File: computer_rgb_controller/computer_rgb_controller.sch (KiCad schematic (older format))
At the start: 19 parts

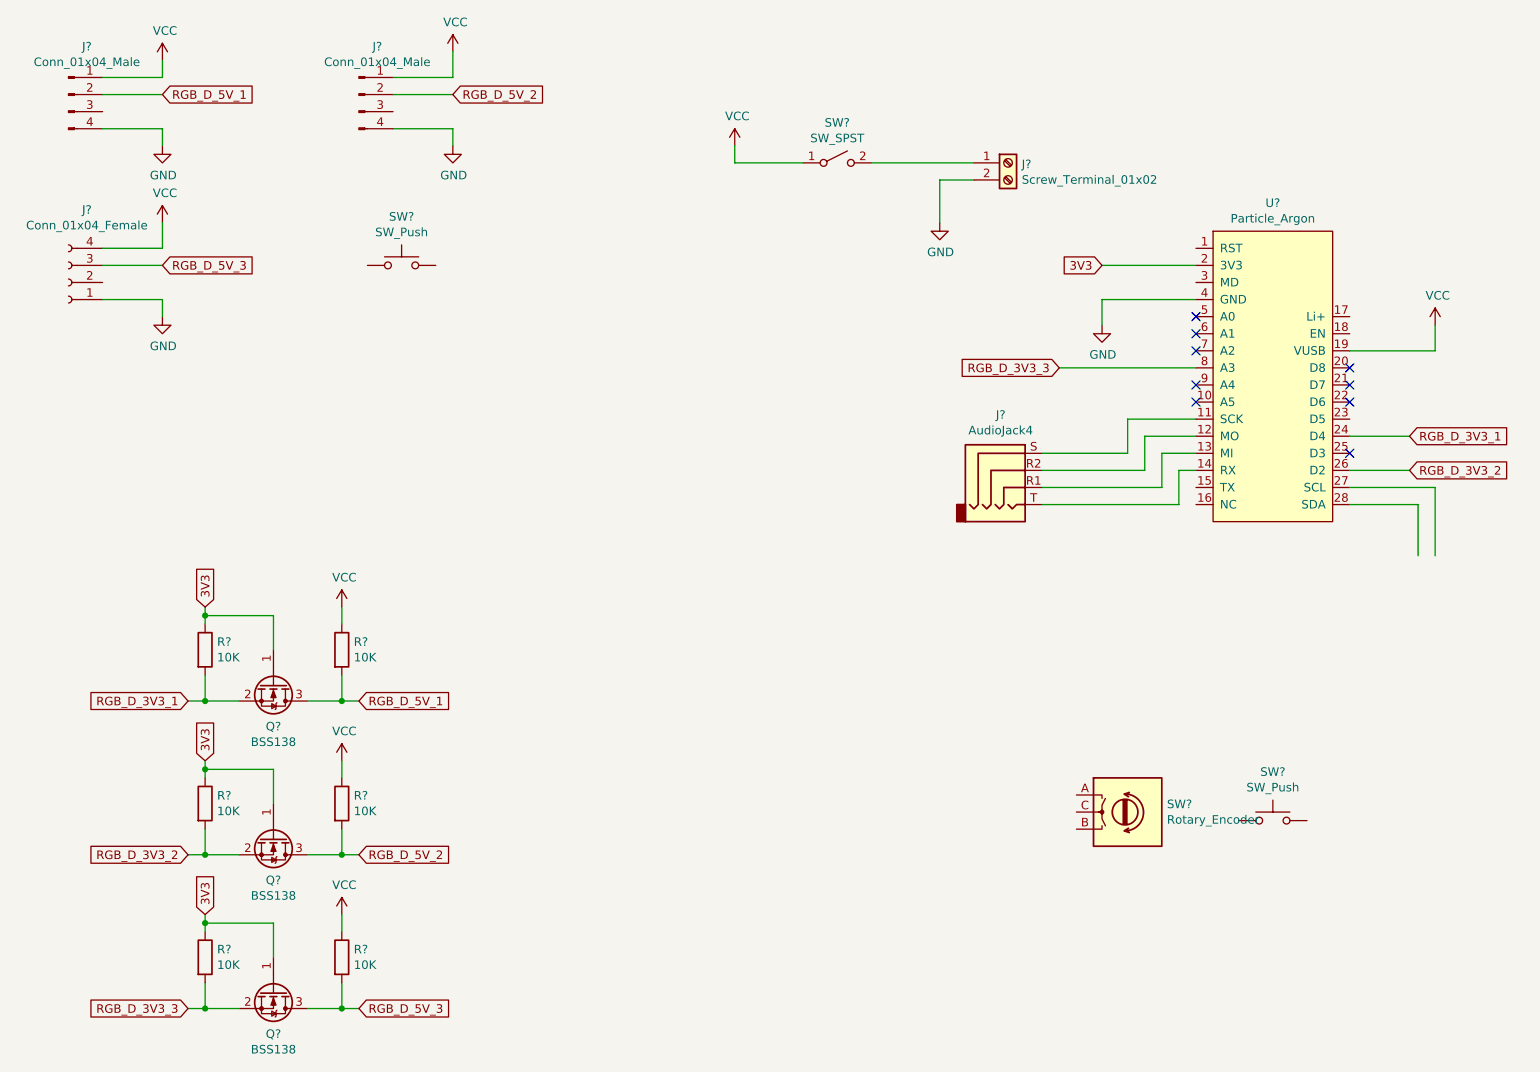
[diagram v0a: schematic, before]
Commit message: added to schematic
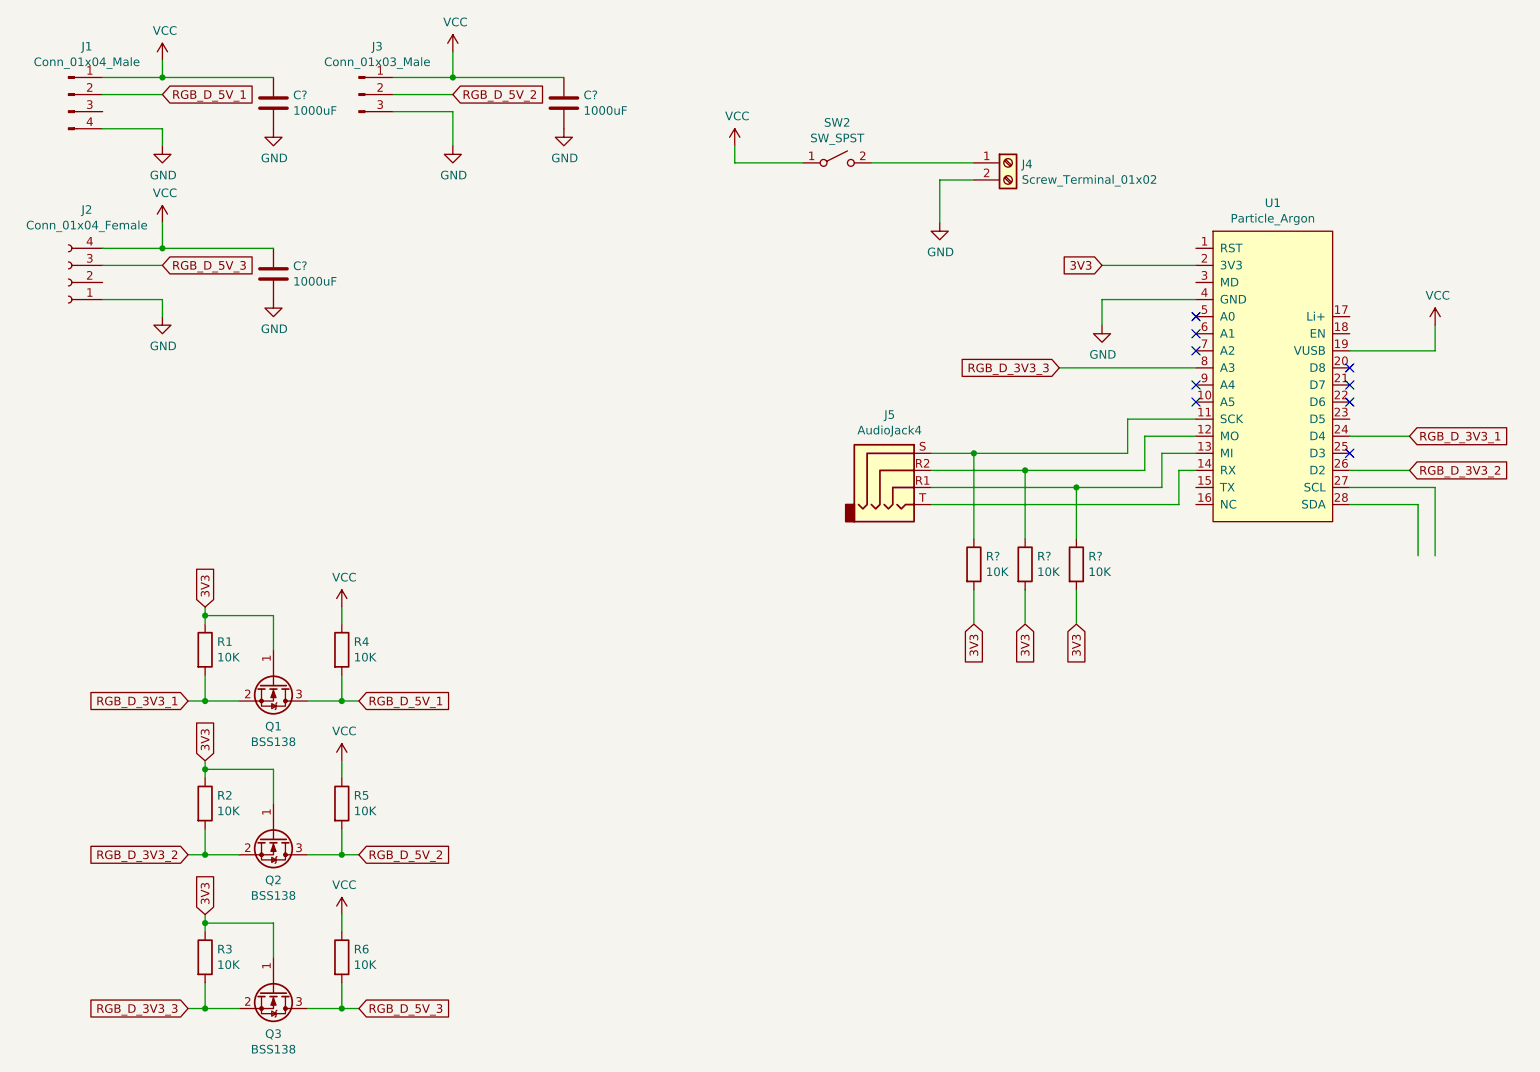
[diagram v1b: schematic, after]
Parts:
- removed J?: Conn_01x04_Male, symbol Connector:Conn_01x04_Male
- removed SW?: Rotary_Encoder, symbol Device:Rotary_Encoder
- removed SW? (x2): SW_Push, symbol Switch:SW_Push
- added C? (x3): 1000uF, symbol Device:C
- added J3: Conn_01x03_Male, Connector_PinHeader_2.54mm:PinHeader_1x03_P2.54mm_Vertical, symbol Connector:Conn_01x03_Male
- added R? (x3): 10K, symbol Device:R
- J1: renamed from J?; footprint (none) -> Connector_PinHeader_2.54mm:PinHeader_1x04_P2.54mm_Vertical
- J2: renamed from J?; footprint (none) -> Connector_PinSocket_2.54mm:PinSocket_1x04_P2.54mm_Vertical
- J4: renamed from J?; footprint (none) -> TerminalBlock:TerminalBlock_bornier-2_P5.08mm
- R1, R2, R3, R4, R5, R6: renamed from R?; footprint (none) -> Resistor_SMD:R_1206_3216Metric_Pad1.30x1.75mm_HandSolder
- U1: renamed from U?; footprint (none) -> Particle_argon:Particle_Argon
- gave numbers to parts that had none: 5
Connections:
- net 3V3: now also R?.2, R?.2, R?.2
- net GND: now also C?.2, C?.2, C?.2, J3.3 (Pin_3)
- net RGB_D_5V_2: now also J3.2 (Pin_2)
- net VCC: now also C?.1, C?.1, C?.1, J3.1 (Pin_1)
- net at J5.S, U1.11 (SCK): now also R?.1
- net at J5.R2, U1.12 (MO): now also R?.1
- net at J5.R1, U1.13 (MI): now also R?.1
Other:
- moved on the sheet: J5

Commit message: modified connector location to avoid clerance issues
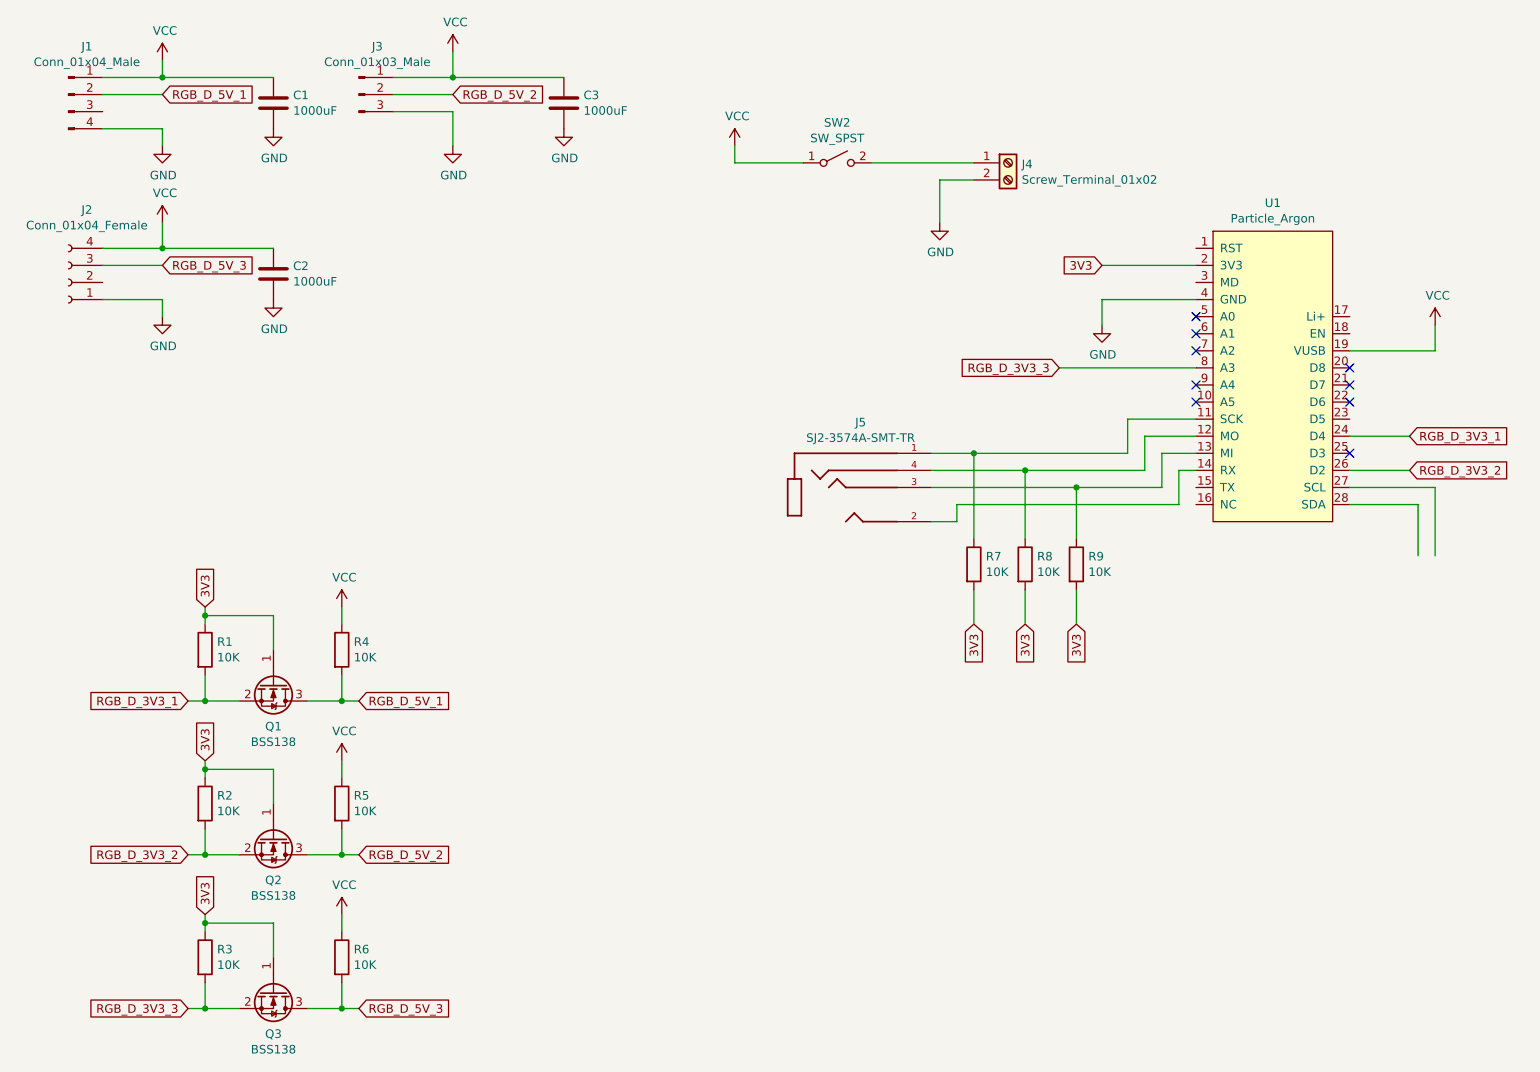
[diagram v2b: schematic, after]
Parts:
- removed J5: AudioJack4, symbol Connector:AudioJack4
- added J5: SJ2-3574A-SMT-TR, extra:CUI_SJ2-3574A-SMT-TR, symbol SJ2-3574A-SMT-TR:SJ2-3574A-SMT-TR
- C1, C2, C3: renamed from C?; footprint (none) -> Capacitor_THT:CP_Radial_D10.0mm_P5.00mm
- R7, R8, R9: renamed from R?; footprint (none) -> Resistor_SMD:R_1206_3216Metric_Pad1.30x1.75mm_HandSolder
- SW2: footprint (none) -> extra:rocker_sw
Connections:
- net at R7.1, U1.11 (SCK): now also J5.1
- net at R8.1, U1.12 (MO): now also J5.4
- net at R9.1, U1.13 (MI): now also J5.3
- net at U1.14 (RX): now also J5.2
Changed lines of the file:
@@
 F 0 "SW2" H 5600 2185 50  0000 C CNN
 F 1 "SW_SPST" H 5600 2094 50  0000 C CNN
-F 2 "" H 5600 1950 50  0001 C CNN
+F 2 "extra:rocker_sw" H 5600 1950 50  0001 C CNN
 F 3 "~" H 5600 1950 50  0001 C CNN
 	1    5600 1950
-	1    0    0    -1
-$EndComp
-$Comp
-L Connector:AudioJack4 J5
-U 1 1 5F9C2744
-P 5950 3750
-F 0 "J5" H 5907 4075 50  0000 C CNN
-F 1 "AudioJack4" H 5907 3984 50  0000 C CNN
-F 2 "" H 5950 3750 50  0001 C CNN
-F 3 "~" H 5950 3750 50  0001 C CNN
-	1    5950 3750
 	1    0    0    -1
 $EndComp
@@
 Connection ~ 1650 2450
 $Comp
-L Device:C C?
+L Device:C C1
 U 1 1 5FA12FC3
 P 2300 1600
-F 0 "C?" H 2415 1646 50  0000 L CNN
+F 0 "C1" H 2415 1646 50  0000 L CNN
 F 1 "1000uF" H 2415 1555 50  0000 L CNN
-F 2 "" H 2338 1450 50  0001 C CNN
+F 2 "Capacitor_THT:CP_Radial_D10.0mm_P5.00mm" H 2338 1450 50  0001 C CNN
 F 3 "~" H 2300 1600 50  0001 C CNN
 	1    2300 1600
@@
 $EndComp
 $Comp
-L Device:C C?
+L Device:C C3
 U 1 1 5FA149B1
 P 4000 1600
-F 0 "C?" H 4115 1646 50  0000 L CNN
+F 0 "C3" H 4115 1646 50  0000 L CNN
 F 1 "1000uF" H 4115 1555 50  0000 L CNN
-F 2 "" H 4038 1450 50  0001 C CNN
+F 2 "Capacitor_THT:CP_Radial_D10.0mm_P5.00mm" H 4038 1450 50  0001 C CNN
 F 3 "~" H 4000 1600 50  0001 C CNN
 	1    4000 1600
@@
 $EndComp
 $Comp
-L Device:C C?
+L Device:C C2
 U 1 1 5FA156F8
 P 2300 2600
-F 0 "C?" H 2415 2646 50  0000 L CNN
+F 0 "C2" H 2415 2646 50  0000 L CNN
 F 1 "1000uF" H 2415 2555 50  0000 L CNN
-F 2 "" H 2338 2450 50  0001 C CNN
+F 2 "Capacitor_THT:CP_Radial_D10.0mm_P5.00mm" H 2338 2450 50  0001 C CNN
 F 3 "~" H 2300 2600 50  0001 C CNN
 	1    2300 2600
@@
 $EndComp
 $Comp
-L power:GND #PWR?
+L power:GND #PWR0114
 U 1 1 5FA161C2
 P 2300 2750
-F 0 "#PWR?" H 2300 2500 50  0001 C CNN
+F 0 "#PWR0114" H 2300 2500 50  0001 C CNN
 F 1 "GND" H 2305 2577 50  0000 C CNN
 F 2 "" H 2300 2750 50  0001 C CNN
@@
 $EndComp
 $Comp
-L power:GND #PWR?
+L power:GND #PWR0115
 U 1 1 5FA16926
 P 4000 1750
-F 0 "#PWR?" H 4000 1500 50  0001 C CNN
+F 0 "#PWR0115" H 4000 1500 50  0001 C CNN
 F 1 "GND" H 4005 1577 50  0000 C CNN
 F 2 "" H 4000 1750 50  0001 C CNN
@@
 $EndComp
 $Comp
-L power:GND #PWR?
+L power:GND #PWR0116
 U 1 1 5FA17BDE
 P 2300 1750
-F 0 "#PWR?" H 2300 1500 50  0001 C CNN
+F 0 "#PWR0116" H 2300 1500 50  0001 C CNN
 F 1 "GND" H 2305 1577 50  0000 C CNN
 F 2 "" H 2300 1750 50  0001 C CNN
@@
 Wire Wire Line
 	6400 3650 7300 3650
-Wire Wire Line
-	6150 3950 7600 3950
-$Comp
-L Device:R R?
+$Comp
+L Device:R R7
 U 1 1 5FA3D413
 P 6400 4300
-F 0 "R?" H 6470 4346 50  0000 L CNN
+F 0 "R7" H 6470 4346 50  0000 L CNN
 F 1 "10K" H 6470 4255 50  0000 L CNN
-F 2 "" V 6330 4300 50  0001 C CNN
+F 2 "Resistor_SMD:R_1206_3216Metric_Pad1.30x1.75mm_HandSolder" V 6330 4300 50  0001 C CNN
 F 3 "~" H 6400 4300 50  0001 C CNN
 	1    6400 4300
@@
 $EndComp
 $Comp
-L Device:R R?
+L Device:R R8
 U 1 1 5FA3DD9C
 P 6700 4300
-F 0 "R?" H 6770 4346 50  0000 L CNN
+F 0 "R8" H 6770 4346 50  0000 L CNN
 F 1 "10K" H 6770 4255 50  0000 L CNN
-F 2 "" V 6630 4300 50  0001 C CNN
+F 2 "Resistor_SMD:R_1206_3216Metric_Pad1.30x1.75mm_HandSolder" V 6630 4300 50  0001 C CNN
 F 3 "~" H 6700 4300 50  0001 C CNN
 	1    6700 4300
@@
 $EndComp
 $Comp
-L Device:R R?
+L Device:R R9
 U 1 1 5FA3E1F2
 P 7000 4300
-F 0 "R?" H 7070 4346 50  0000 L CNN
+F 0 "R9" H 7070 4346 50  0000 L CNN
 F 1 "10K" H 7070 4255 50  0000 L CNN
-F 2 "" V 6930 4300 50  0001 C CNN
+F 2 "Resistor_SMD:R_1206_3216Metric_Pad1.30x1.75mm_HandSolder" V 6930 4300 50  0001 C CNN
 F 3 "~" H 7000 4300 50  0001 C CNN
 	1    7000 4300
@@
 Text GLabel 6400 4650 3    50   Input ~ 0
 3V3
+$Comp
+L SJ2-3574A-SMT-TR:SJ2-3574A-SMT-TR J5
+U 1 1 5FB06BBA
+P 5650 3850
+F 0 "J5" H 5737 4231 50  0000 C CNN
+F 1 "SJ2-3574A-SMT-TR" H 5737 4140 50  0000 C CNN
+F 2 "extra:CUI_SJ2-3574A-SMT-TR" H 5650 3850 50  0001 L BNN
+F 3 "" H 5650 3850 50  0001 L BNN
+F 4 "Manufacturer Recommendations" H 5650 3850 50  0001 L BNN "STANDARD"
+F 5 "5.3 mm" H 5650 3850 50  0001 L BNN "MAXIMUM_PACKAGE_HEIGHT"
+F 6 "CUI" H 5650 3850 50  0001 L BNN "MANUFACTURER"
+F 7 "1.02" H 5650 3850 50  0001 L BNN "PARTREV"
+	1    5650 3850
+	1    0    0    -1
+$EndComp
+Wire Wire Line
+	6300 3950 6300 4050
+Wire Wire Line
+	6300 4050 6150 4050
+Wire Wire Line
+	6300 3950 7600 3950
 $EndSCHEMATC

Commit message: updated trrs jack, old one was out of stock :(
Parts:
- J5: footprint extra:CUI_SJ2-3574A-SMT-TR -> extra:CUI_SJ2-35043A-SMT-TR
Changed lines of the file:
@@
 F 0 "J5" H 5737 4231 50  0000 C CNN
 F 1 "SJ2-3574A-SMT-TR" H 5737 4140 50  0000 C CNN
-F 2 "extra:CUI_SJ2-3574A-SMT-TR" H 5650 3850 50  0001 L BNN
+F 2 "extra:CUI_SJ2-35043A-SMT-TR" H 5650 3850 50  0001 L BNN
 F 3 "" H 5650 3850 50  0001 L BNN
 F 4 "Manufacturer Recommendations" H 5650 3850 50  0001 L BNN "STANDARD"

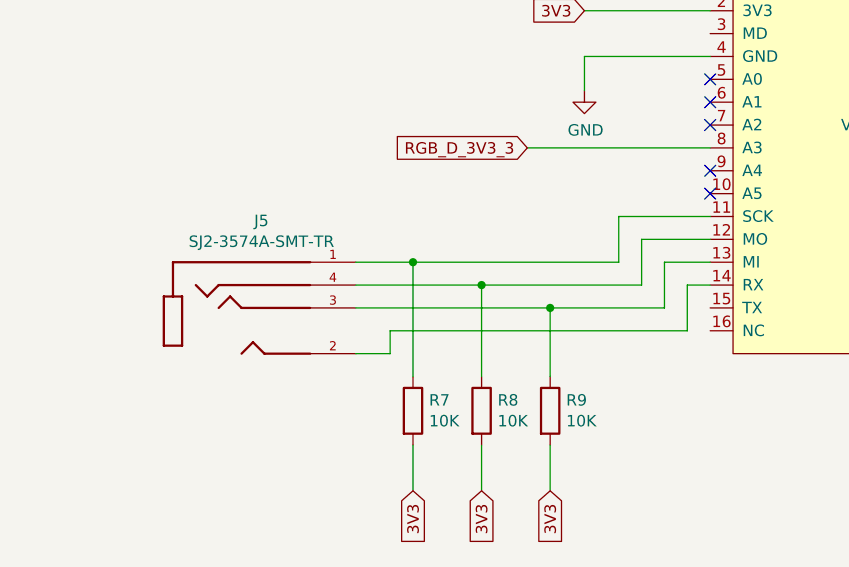
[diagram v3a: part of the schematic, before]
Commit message: updated TRRS jack bc previous one was wrong one
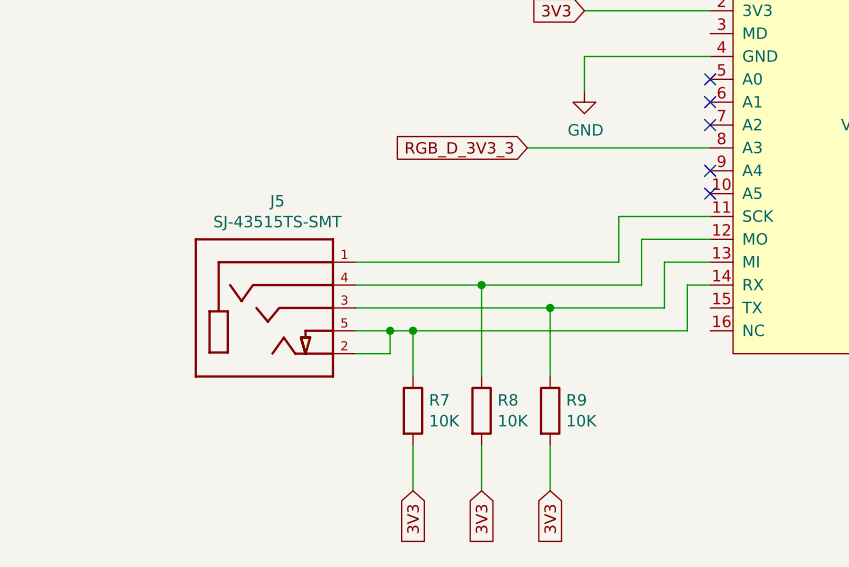
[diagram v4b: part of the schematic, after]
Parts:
- removed J5: SJ2-3574A-SMT-TR, extra:CUI_SJ2-35043A-SMT-TR, symbol SJ2-3574A-SMT-TR:SJ2-3574A-SMT-TR
- added J5: SJ-43515TS-SMT, extra:CUI_SJ-43515TS-SMT, symbol SJ-43515TS-SMT:SJ-43515TS-SMT
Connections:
- net at U1.11 (SCK): now also J5.1; no longer R7.1
- net at R8.1, U1.12 (MO): now also J5.4
- net at R9.1, U1.13 (MI): now also J5.3
- net at U1.14 (RX): now also R7.1, J5.2, J5.5
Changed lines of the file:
@@
 	1    0    0    -1
 $EndComp
-Wire Wire Line
-	6150 3650 6400 3650
-Wire Wire Line
-	6400 3650 6400 4150
-Connection ~ 6400 3650
-Wire Wire Line
-	6400 3650 7300 3650
 $Comp
 L Device:R R7
@@
 Text GLabel 6400 4650 3    50   Input ~ 0
 3V3
-$Comp
-L SJ2-3574A-SMT-TR:SJ2-3574A-SMT-TR J5
-U 1 1 5FB06BBA
-P 5650 3850
-F 0 "J5" H 5737 4231 50  0000 C CNN
-F 1 "SJ2-3574A-SMT-TR" H 5737 4140 50  0000 C CNN
-F 2 "extra:CUI_SJ2-35043A-SMT-TR" H 5650 3850 50  0001 L BNN
-F 3 "" H 5650 3850 50  0001 L BNN
-F 4 "Manufacturer Recommendations" H 5650 3850 50  0001 L BNN "STANDARD"
-F 5 "5.3 mm" H 5650 3850 50  0001 L BNN "MAXIMUM_PACKAGE_HEIGHT"
-F 6 "CUI" H 5650 3850 50  0001 L BNN "MANUFACTURER"
-F 7 "1.02" H 5650 3850 50  0001 L BNN "PARTREV"
-	1    5650 3850
-	1    0    0    -1
-$EndComp
 Wire Wire Line
 	6300 3950 6300 4050
@@
 	6300 4050 6150 4050
 Wire Wire Line
-	6300 3950 7600 3950
+	6300 3950 6400 3950
+Wire Wire Line
+	6150 3650 7300 3650
+Wire Wire Line
+	6400 4150 6400 3950
+Connection ~ 6400 3950
+Wire Wire Line
+	6400 3950 7600 3950
+$Comp
+L SJ-43515TS-SMT:SJ-43515TS-SMT J5
+U 1 1 605EDA65
+P 5750 3850
+F 0 "J5" H 5807 4317 50  0000 C CNN
+F 1 "SJ-43515TS-SMT" H 5807 4226 50  0000 C CNN
+F 2 "extra:CUI_SJ-43515TS-SMT" H 5750 3850 50  0001 L BNN
+F 3 "" H 5750 3850 50  0001 L BNN
+F 4 "CUI" H 5750 3850 50  0001 L BNN "MF"
+F 5 "4 conductor 3.5 mm Surface Mount Audio Jack w/ Tip Switch" H 5750 3850 50  0001 L BNN "DESCRIPTION"
+F 6 "SJ-43515TS-SMT" H 5750 3850 50  0001 L BNN "MP"
+F 7 "None" H 5750 3850 50  0001 L BNN "PACKAGE"
+F 8 "None" H 5750 3850 50  0001 L BNN "PRICE"
+F 9 "Unavailable" H 5750 3850 50  0001 L BNN "AVAILABILITY"
+	1    5750 3850
+	1    0    0    -1
+$EndComp
+Wire Wire Line
+	6300 3950 6150 3950
+Connection ~ 6300 3950
 $EndSCHEMATC
